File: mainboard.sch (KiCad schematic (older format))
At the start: 60 parts

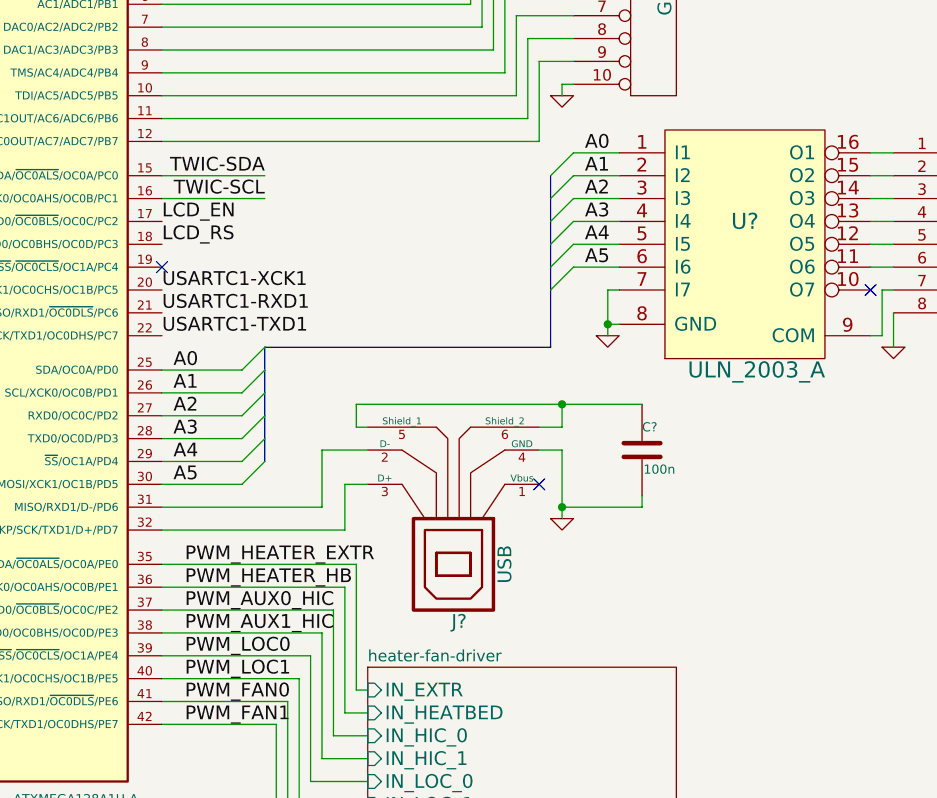
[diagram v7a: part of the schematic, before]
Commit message: Input protection for USB, I2C and USART
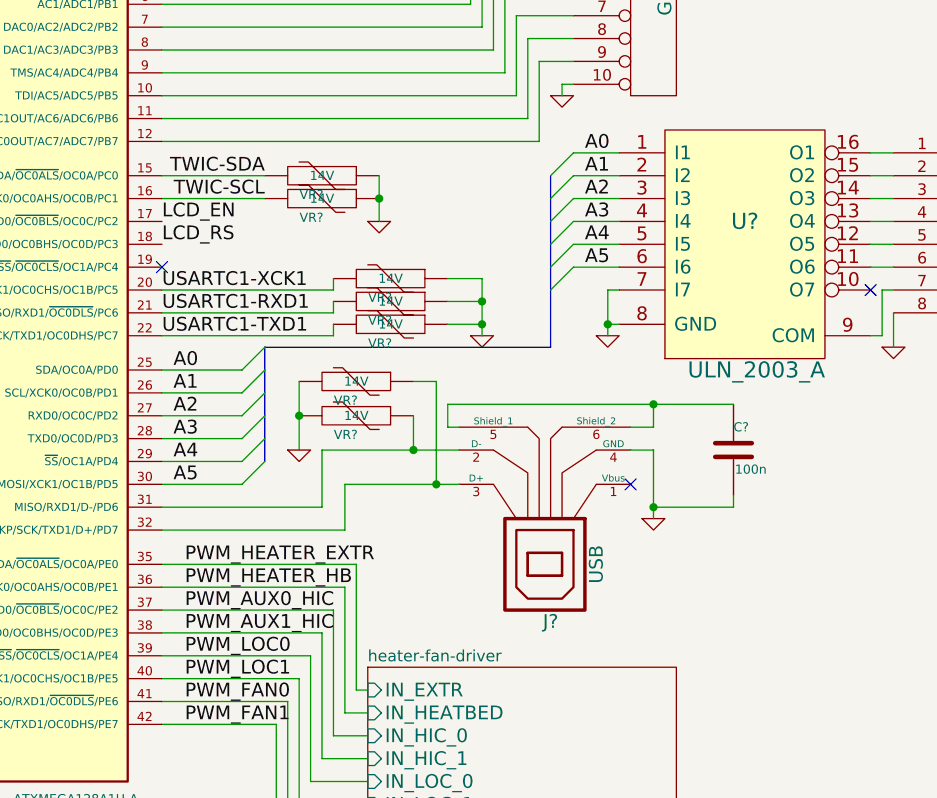
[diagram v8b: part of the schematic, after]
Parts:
- added VR? (x7): 14V, symbol VR
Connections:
- net GND: now also VR?.1, VR?.1, VR?.1, VR?.1, VR?.1, VR?.2, VR?.2
- net TWIC-SCL: now also VR?.2
- net TWIC-SDA: now also VR?.2
- net USARTC1-RXD1: now also VR?.2
- net USARTC1-TXD1: now also VR?.2
- net USARTC1-XCK1: now also VR?.2
- net at IC?.31 (MISO/RXD1/D-/PD6), J?.2 (D-): now also VR?.1
- net at IC?.32 (EVOUT/CLKP/SCK/TXD1/D+/PD7), J?.3 (D+): now also VR?.1
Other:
- moved on the sheet: C?, J?
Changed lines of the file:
@@
 L GND #PWR?
 U 1 1 5333067B
-P 5850 6100
-F 0 "#PWR?" H 5850 6100 30  0001 C CNN
-F 1 "GND" H 5850 6030 30  0001 C CNN
-F 2 "" H 5850 6100 60  0000 C CNN
-F 3 "" H 5850 6100 60  0000 C CNN
-	1    5850 6100
-	1    0    0    -1
-$EndComp
-NoConn ~ 5750 5950
+P 6250 6100
+F 0 "#PWR?" H 6250 6100 30  0001 C CNN
+F 1 "GND" H 6250 6030 30  0001 C CNN
+F 2 "" H 6250 6100 60  0000 C CNN
+F 3 "" H 6250 6100 60  0000 C CNN
+	1    6250 6100
+	1    0    0    -1
+$EndComp
+NoConn ~ 6150 5950
 Text Label 4550 4600 2    60   ~ 0
 TWIC-SDA
@@
 L USB J?
 U 1 1 53330539
-P 5350 6150
-F 0 "J?" H 5300 6550 60  0000 C CNN
-F 1 "USB" V 5100 6300 60  0000 C CNN
-F 2 "" H 5350 6150 60  0000 C CNN
-F 3 "" H 5350 6150 60  0000 C CNN
-	1    5350 6150
+P 5750 6150
+F 0 "J?" H 5700 6550 60  0000 C CNN
+F 1 "USB" V 5500 6300 60  0000 C CNN
+F 2 "" H 5750 6150 60  0000 C CNN
+F 3 "" H 5750 6150 60  0000 C CNN
+	1    5750 6150
 	-1   0    0    1
 $EndComp
@@
 L C C?
 U 1 1 53502E4E
-P 6200 5800
-F 0 "C?" H 6200 5900 40  0000 L CNN
-F 1 "100n" H 6206 5715 40  0000 L CNN
-F 2 "" H 6238 5650 30  0000 C CNN
-F 3 "" H 6200 5800 60  0000 C CNN
-	1    6200 5800
+P 6600 5800
+F 0 "C?" H 6600 5900 40  0000 L CNN
+F 1 "100n" H 6606 5715 40  0000 L CNN
+F 2 "" H 6638 5650 30  0000 C CNN
+F 3 "" H 6600 5800 60  0000 C CNN
+	1    6600 5800
 	1    0    0    -1
 $EndComp
@@
 	800  3650 800  3600
 Wire Wire Line
-	4900 5950 5000 5950
-Wire Wire Line
-	4800 5800 5000 5800
-Wire Wire Line
-	5000 5700 4950 5700
-Wire Wire Line
-	4950 5700 4950 5600
-Wire Wire Line
-	4950 5600 6200 5600
-Wire Wire Line
-	5850 5700 5750 5700
+	4900 5950 5400 5950
+Wire Wire Line
+	4800 5800 5400 5800
+Wire Wire Line
+	5400 5700 5350 5700
+Wire Wire Line
+	5350 5700 5350 5600
+Wire Wire Line
+	5350 5600 6600 5600
+Wire Wire Line
+	6250 5700 6150 5700
 Wire Wire Line
 	4950 6300 4950 6850
@@
 	6050 5100 6100 5100
 Wire Bus Line
-	5800 5350 5800 4600
+	5800 4600 5800 5350
 Wire Wire Line
 	5900 4500 6100 4500
@@
 	7300 5200 7300 5350
 Wire Bus Line
-	4550 5350 5800 5350
-Wire Wire Line
-	5850 6100 5850 5800
-Wire Wire Line
-	5850 5800 5750 5800
-Wire Wire Line
-	5850 6050 6200 6050
-Wire Wire Line
-	6200 6050 6200 6000
-Connection ~ 5850 6050
-Wire Wire Line
-	5850 5700 5850 5600
-Connection ~ 5850 5600
+	5800 5350 4550 5350
+Wire Wire Line
+	6250 5800 6250 6100
+Wire Wire Line
+	6250 5800 6150 5800
+Wire Wire Line
+	6250 6050 6600 6050
+Wire Wire Line
+	6600 6050 6600 6000
+Connection ~ 6250 6050
+Wire Wire Line
+	6250 5700 6250 5600
+Connection ~ 6250 5600
 NoConn ~ 4100 5000
 $Comp
@@
 Connection ~ 5700 1600
 NoConn ~ 1700 3700
+$Comp
+L VR VR?
+U 1 1 535154B3
+P 4950 5650
+F 0 "VR?" V 5010 5604 40  0000 C TNN
+F 1 "14V" V 4950 5650 40  0000 C CNN
+F 2 "" H 4950 5650 60  0000 C CNN
+F 3 "" H 4950 5650 60  0000 C CNN
+	1    4950 5650
+	0    1    1    0
+$EndComp
+$Comp
+L VR VR?
+U 1 1 535154CF
+P 4950 5500
+F 0 "VR?" V 5010 5454 40  0000 C TNN
+F 1 "14V" V 4950 5500 40  0000 C CNN
+F 2 "" H 4950 5500 60  0000 C CNN
+F 3 "" H 4950 5500 60  0000 C CNN
+	1    4950 5500
+	0    1    1    0
+$EndComp
+Wire Wire Line
+	5200 5800 5200 5650
+Connection ~ 5200 5800
+Wire Wire Line
+	5300 5950 5300 5500
+Wire Wire Line
+	5300 5500 5200 5500
+Connection ~ 5300 5950
+$Comp
+L GND #PWR?
+U 1 1 535158E5
+P 4700 5800
+F 0 "#PWR?" H 4700 5800 30  0001 C CNN
+F 1 "GND" H 4700 5730 30  0001 C CNN
+F 2 "" H 4700 5800 60  0000 C CNN
+F 3 "" H 4700 5800 60  0000 C CNN
+	1    4700 5800
+	1    0    0    -1
+$EndComp
+Wire Wire Line
+	4700 5500 4700 5800
+Connection ~ 4700 5650
+$Comp
+L VR VR?
+U 1 1 535160AF
+P 4800 4600
+F 0 "VR?" V 4860 4554 40  0000 C TNN
+F 1 "14V" V 4800 4600 40  0000 C CNN
+F 2 "" H 4800 4600 60  0000 C CNN
+F 3 "" H 4800 4600 60  0000 C CNN
+	1    4800 4600
+	0    1    1    0
+$EndComp
+$Comp
+L VR VR?
+U 1 1 535160BA
+P 4800 4700
+F 0 "VR?" V 4860 4654 40  0000 C TNN
+F 1 "14V" V 4800 4700 40  0000 C CNN
+F 2 "" H 4800 4700 60  0000 C CNN
+F 3 "" H 4800 4700 60  0000 C CNN
+	1    4800 4700
+	0    1    1    0
+$EndComp
+$Comp
+L GND #PWR?
+U 1 1 535160C5
+P 5050 4800
+F 0 "#PWR?" H 5050 4800 30  0001 C CNN
+F 1 "GND" H 5050 4730 30  0001 C CNN
+F 2 "" H 5050 4800 60  0000 C CNN
+F 3 "" H 5050 4800 60  0000 C CNN
+	1    5050 4800
+	1    0    0    -1
+$EndComp
+Wire Wire Line
+	5050 4600 5050 4800
+Connection ~ 5050 4700
+$Comp
+L GND #PWR?
+U 1 1 53516604
+P 5500 5300
+F 0 "#PWR?" H 5500 5300 30  0001 C CNN
+F 1 "GND" H 5500 5230 30  0001 C CNN
+F 2 "" H 5500 5300 60  0000 C CNN
+F 3 "" H 5500 5300 60  0000 C CNN
+	1    5500 5300
+	1    0    0    -1
+$EndComp
+$Comp
+L VR VR?
+U 1 1 5351660F
+P 5100 5050
+F 0 "VR?" V 5160 5004 40  0000 C TNN
+F 1 "14V" V 5100 5050 40  0000 C CNN
+F 2 "" H 5100 5050 60  0000 C CNN
+F 3 "" H 5100 5050 60  0000 C CNN
+	1    5100 5050
+	0    1    1    0
+$EndComp
+$Comp
+L VR VR?
+U 1 1 53516624
+P 5100 5150
+F 0 "VR?" V 5160 5104 40  0000 C TNN
+F 1 "14V" V 5100 5150 40  0000 C CNN
+F 2 "" H 5100 5150 60  0000 C CNN
+F 3 "" H 5100 5150 60  0000 C CNN
+	1    5100 5150
+	0    1    1    0
+$EndComp
+$Comp
+L VR VR?
+U 1 1 5351662F
+P 5100 5250
+F 0 "VR?" V 5160 5204 40  0000 C TNN
+F 1 "14V" V 5100 5250 40  0000 C CNN
+F 2 "" H 5100 5250 60  0000 C CNN
+F 3 "" H 5100 5250 60  0000 C CNN
+	1    5100 5250
+	0    1    1    0
+$EndComp
+Wire Wire Line
+	5500 5300 5500 5050
+Wire Wire Line
+	5500 5050 5350 5050
+Wire Wire Line
+	5350 5150 5500 5150
+Connection ~ 5500 5150
+Wire Wire Line
+	5350 5250 5500 5250
+Connection ~ 5500 5250
+Wire Wire Line
+	4850 5050 4850 5100
+Wire Wire Line
+	4850 5100 4100 5100
+Wire Wire Line
+	4850 5150 4850 5200
+Wire Wire Line
+	4850 5200 4100 5200
+Wire Wire Line
+	4850 5250 4850 5300
+Wire Wire Line
+	4850 5300 4100 5300
 $EndSCHEMATC
